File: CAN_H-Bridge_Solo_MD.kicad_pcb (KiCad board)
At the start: 2 copper layers, 84.3 x 40.1 mm, 47 parts, among them IC2 SI8650AB-B-IS1, IC3 A3921KLPTR-T, J1 Conn_01x03, J2 Conthrough, J3 Bus_mechaken_PCIexpress_x16_1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, J4 Conn_01x05, M1 Motor_DC, Q1 TK6R7P06PLRQ, Q2 TK6R7P06PLRQ, Q3 TK6R7P06PLRQ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

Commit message: Update: 配線の修正
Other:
- board text added: "5V"
- board text added: "A"
- board text added: "B"
- board text added: "X"

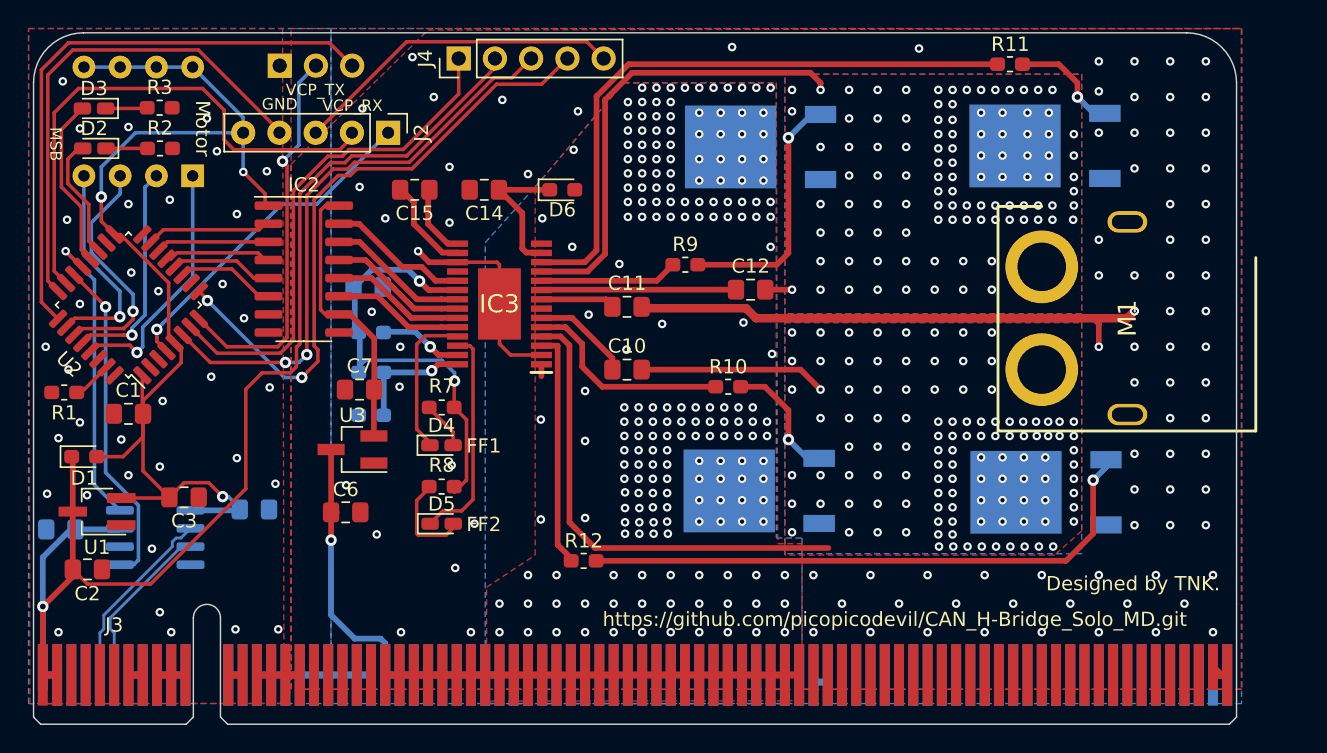
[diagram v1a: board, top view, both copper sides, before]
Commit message: Update: シルク配置を上側に変更
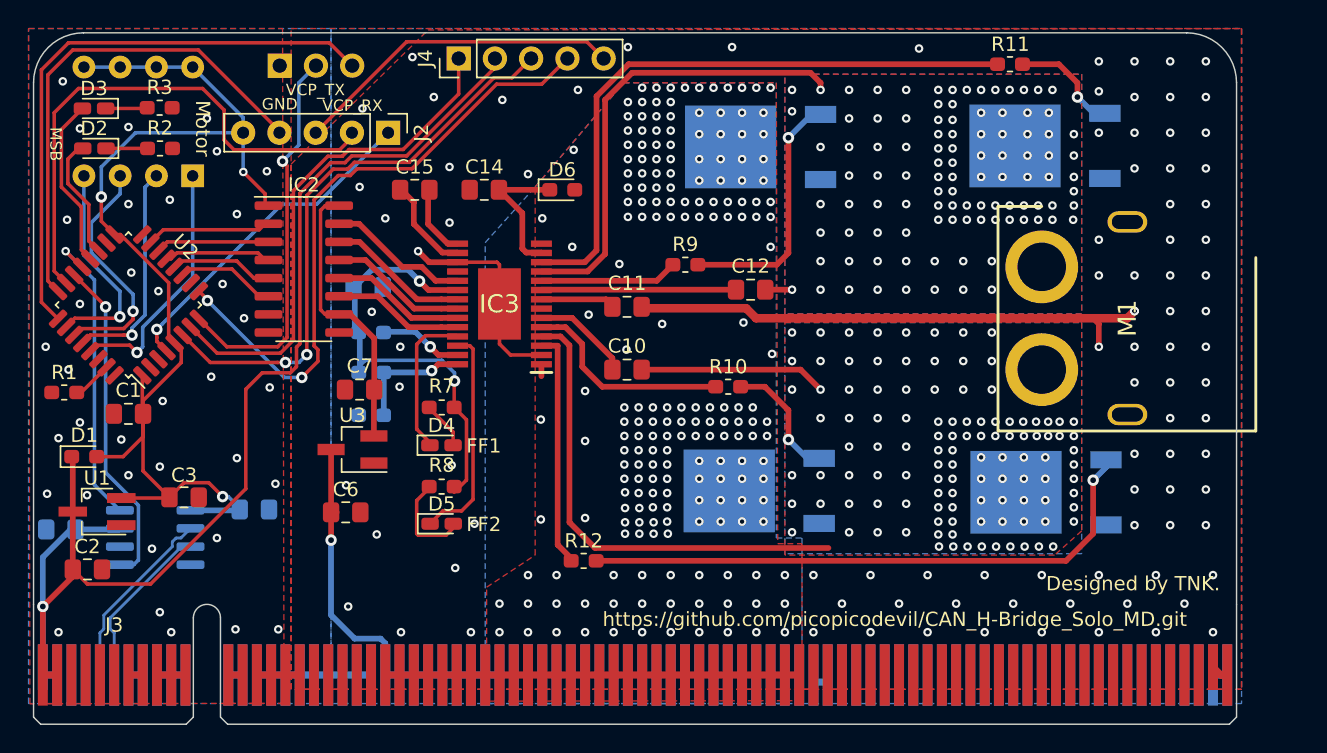
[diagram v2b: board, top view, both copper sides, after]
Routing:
- net GNDPWR: vias 92 -> 94
- net GND: vias 35 -> 36

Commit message: Update: MCUをF042K6からF303K8へ変更
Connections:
- IC2 pad 7: Net-(IC2-Pad7) -> (no net)
- IC3 pad 14: Net-(IC3-Pad14) -> (no net)
- IC3 pad 18: Net-(IC3-Pad18) -> (no net)
- IC3 pad 7: Net-(IC3-Pad7) -> (no net)
- J3 pad B3: Net-(J3-PadB3) -> (no net)
- J3 pad B4: Net-(J3-PadB4) -> (no net)
- U2 pad 10: Net-(U2-Pad10) -> (no net)
- U2 pad 18: Net-(U2-Pad18) -> (no net)
- U2 pad 2: Net-(U2-Pad2) -> (no net)
- U2 pad 3: Net-(U2-Pad3) -> (no net)
- U2 pad 30: Net-(U2-Pad30) -> (no net)
